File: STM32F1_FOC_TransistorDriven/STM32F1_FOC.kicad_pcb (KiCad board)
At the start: 2 copper layers, 96.7 x 45 mm, 224 parts, among them IC1 MP9486A, J1 Screw_Terminal_01x01, J11 Screw_Terminal_01x01, J12 Screw_Terminal_01x01, J13 Conn_01x03, J14 Screw_Terminal_01x01, J15 Screw_Terminal_01x01, J17 Conn_01x03, J18 Conn_01x03, J19 Conn_01x04, J2 Conn_01x05, J20 Conn_01x03, J21 Conn_01x05, J4 Screw_Terminal_01x01, J5 Screw_Terminal_01x01, J6 Screw_Terminal_01x01, Q1 DMN62D0UW-7, Q10 IRF540N, Q12 MMBT5551L, Q13 SS8050, Q15 SS8550, Q16 SS8550, Q17 SS8550, Q18 SS8550, Q19 IRF540N, Q20 IRF540N, Q3 MMBT5551L, Q32 MMBT5551L, Q33 SS8050, Q34 SS8550, Q35 SS8550, Q36 SS8550, Q37 SS8550, Q38 IRF540N, Q39 IRF540N, Q4 SS8050, Q5 SS8550, Q6 SS8550, Q7 SS8550, Q8 SS8550, Q9 IRF540N, U1 STM32F103C8Tx, U2 AMS1117-5.0, U3 LM1117DT-3.3, U4 INA181, U5 INA181, U6 INA181, U7 INA181

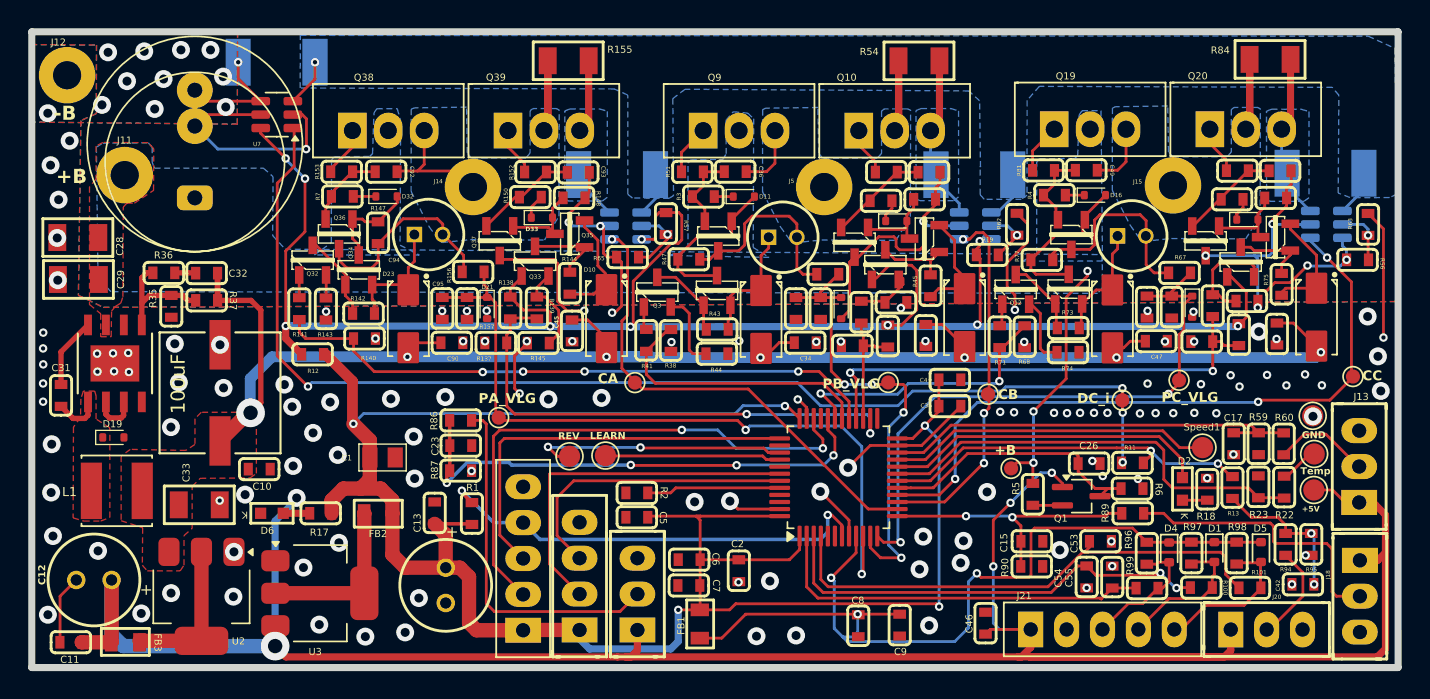
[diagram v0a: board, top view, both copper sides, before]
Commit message: Design 4 layer Board with separate supply and ground plane
Note:
Below points WIP...
-Need to check all the plane.
-Place ground via if needed near to shunt and return path of the supply.
-Validate the layout.
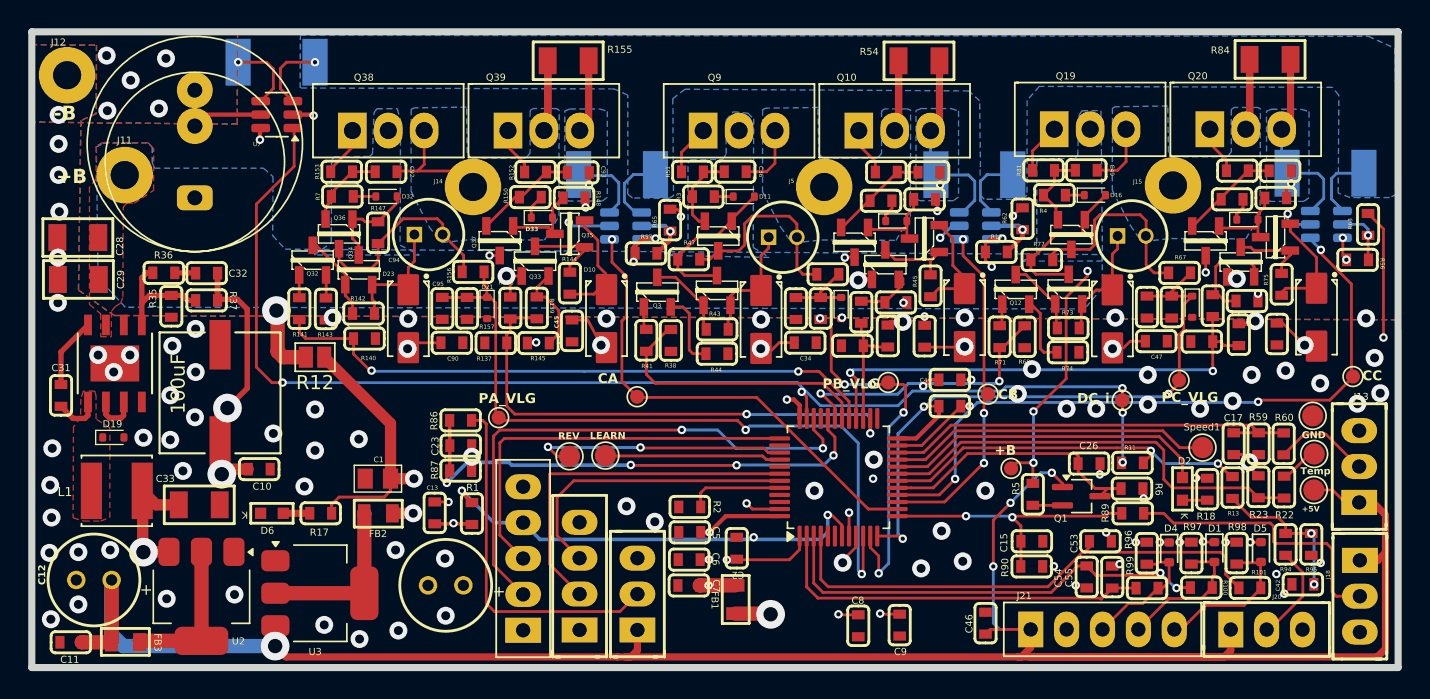
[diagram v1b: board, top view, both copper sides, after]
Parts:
- R12: footprint Footprints:R_0603 -> Jumper:SolderJumper-2_P1.3mm_Open_Pad1.0x1.5mm
- moved R65 4.12 mm to (204.1, 35.0), turned to 90 degrees
- moved C5 3.90 mm to (206.2, 57.1)
- moved R2 3.88 mm to (206.3, 54.5)
- moved FB1 3.06 mm to (209.6, 61.8)
- moved R57 2.51 mm to (203.2, 36.6), turned to 0 degrees
- moved C2 1.65 mm to (209.6, 58.2), turned to 90 degrees
- moved C1 1.54 mm to (184.2, 53.3), turned to 180 degrees
- moved PA_VLG 1.01 mm to (202.6, 47.5)
- moved R12 0.97 mm to (179.8, 44.7), turned to 180 degrees
- moved R19 0.67 mm to (228.0, 36.5)
- moved R62 0.55 mm to (229.1, 34.9)
- turned C18 to 0 degrees
- turned C21 to 90 degrees
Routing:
- net Trasistor_supply: track 136.8 -> 32.0 mm, vias 12 -> 13
- net +3.3VDC: track 150.3 -> 47.9 mm, vias 5 -> 10
- net +12VDC: track 120.2 -> 44.3 mm, vias 7 -> 9
- net GND: track 132.7 -> 61.3 mm, vias 147 -> 114
- net +3.3VDC_FILT: track 63.3 -> 12.3 mm, vias 3 -> 10
- net +5VDC: track 173.6 -> 162.2 mm, vias 5 -> 4
- net M_GND: track 13.7 -> 21.4 mm
- net Phase_Current: track 33.0 -> 39.0 mm
- net Net-(U1-BOOT0): track 9.48 -> 6.73 mm
- net DC_i: track 84.1 -> 86.4 mm
- net CB: track 25.8 -> 24.0 mm
- net Net-(U6-REF): track 4.77 -> 4.15 mm
- net PhaseB_Voltage: track 32.6 -> 33.2 mm
- net Net-(D11-A): track 11.7 -> 11.2 mm
- net PHA_H: track 43.6 -> 43.7 mm, vias 4 -> 2
- added copper zone on In2.Cu, net +12VDC
- added copper zone on In2.Cu, net +3.3VDC
- added copper zone on In2.Cu, net +3.3VDC_FILT
- added copper zone on In1.Cu, net GND
- added copper zone on In2.Cu, net Trasistor_supply
- removed copper zone on F.Cu, net +12VDC
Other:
- copper layers 2 -> 4
